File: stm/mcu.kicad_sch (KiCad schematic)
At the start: 33 parts, among them J1 Conn_02x07_Odd_Even, SW2 SW_Push, U1 REF4132B25DBVR, U2 STM32H730ZBTx, Y3 Crystal_GND24, Y4 Crystal

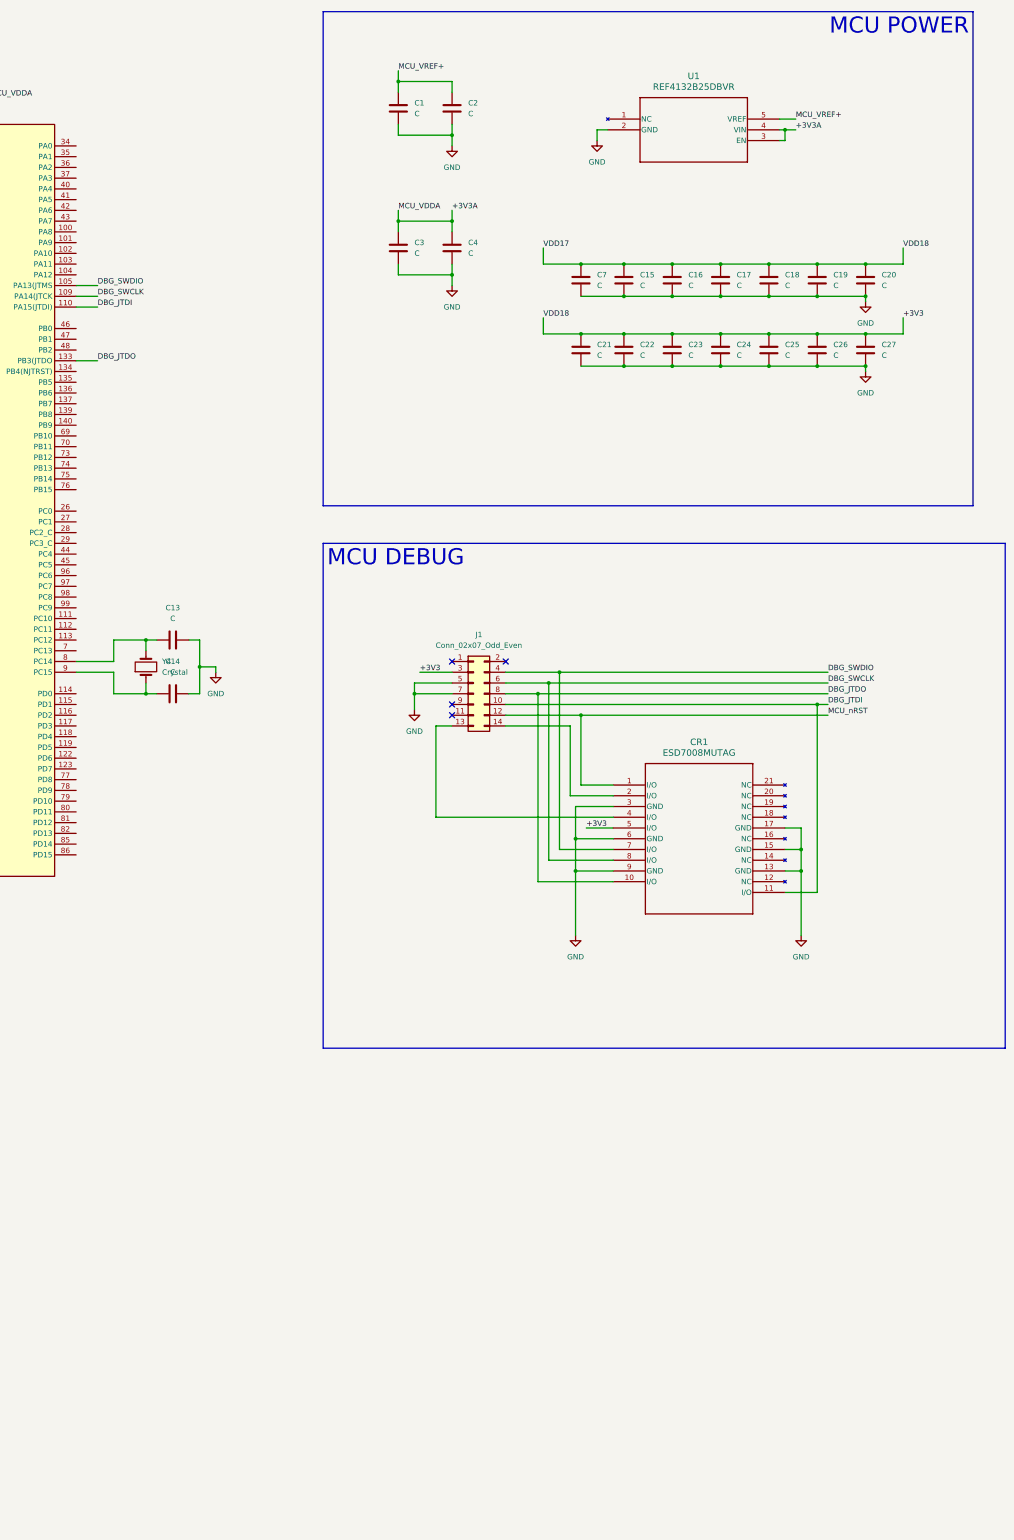
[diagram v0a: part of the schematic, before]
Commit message: STM MCU SD Card
Implemented SD card for external memory.
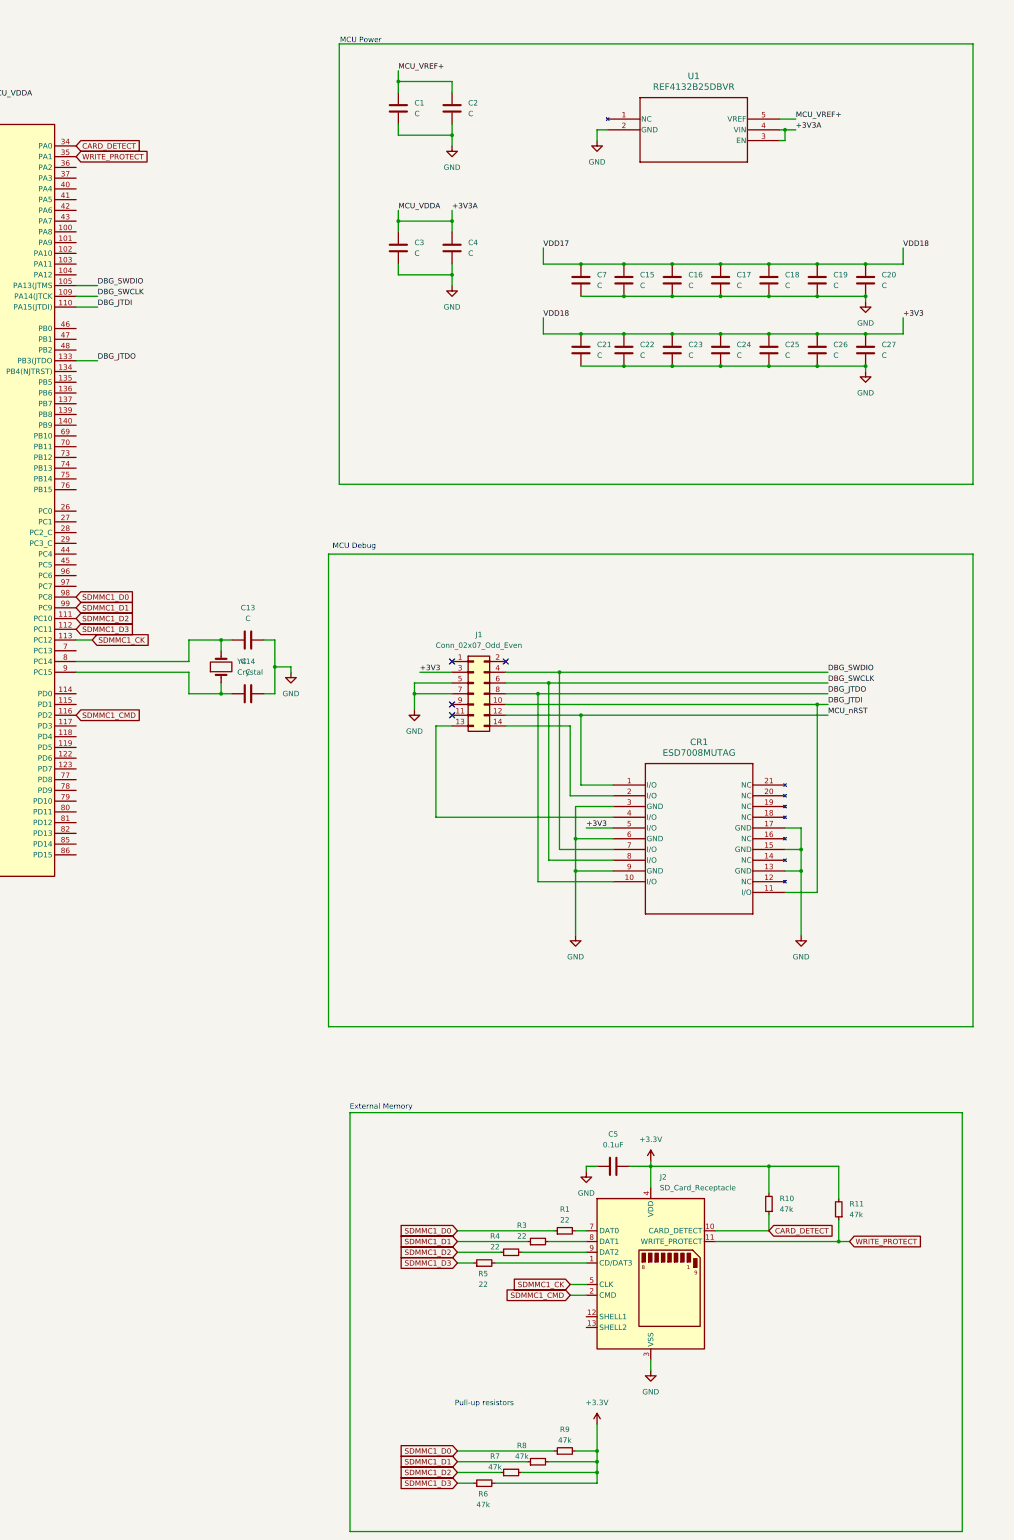
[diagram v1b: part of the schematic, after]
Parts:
- added C5: 0.1uF, symbol Device:C
- added J2: SD_Card_Receptacle, symbol Connector:SD_Card_Receptacle
- added R1, R3, R4, R5: 22, symbol Device:R_Small
- added R10, R11, R6, R7, R8, R9: 47k, symbol Device:R_Small
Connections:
- net GND: now also C5.1, J2.3 (VSS), J2.6 (VSS)
- net SDMMC1_D2: now reaches U2.111 (PC10)
- net SDMMC1_D2: now also R4.1, R7.1
- net SDMMC1_D3: now reaches U2.112 (PC11)
- net SDMMC1_D3: now also R5.1, R6.1
- net SDMMC1_CK: now reaches U2.113 (PC12)
- net SDMMC1_CK: now also J2.5 (CLK)
- net SDMMC1_CMD: now reaches U2.116 (PD2)
- net SDMMC1_CMD: now also J2.2 (CMD)
- net CARD_DETECT: now reaches U2.34 (PA0)
- net CARD_DETECT: now also J2.10 (CARD_DETECT), R10.1
- net WRITE_PROTECT: now reaches U2.35 (PA1)
- net WRITE_PROTECT: now also J2.11 (WRITE_PROTECT), R11.1
- net SDMMC1_D0: now reaches U2.98 (PC8)
- net SDMMC1_D0: now also R1.1, R9.1
- net SDMMC1_D1: now reaches U2.99 (PC9)
- net SDMMC1_D1: now also R3.1, R8.1
- new net: J2.1 (CD/DAT3), R5.2
- new net: J2.7 (DAT0), R1.2
- new net: J2.8 (DAT1), R3.2
- new net: J2.9 (DAT2), R4.2
- new net +3.3V: C5.2, J2.4 (VDD), R10.2, R11.2, R6.2, R7.2, R8.2, R9.2
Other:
- note added: "External Memory"
- note added: "MCU Debug"
- note added: "MCU Power"
- note added: "Pull-up resistors"
- moved on the sheet: C13, C14, Y4

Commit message: ethernet phy
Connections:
- net WRITE_PROTECT: now also U2.56 (PG0); no longer U2.35 (PA1)
- net ETH_MDC: now reaches U2.27 (PC1)
- net ETH_MDIO: now reaches U2.36 (PA2)
- net ETH_CRS_DV: now reaches U2.43 (PA7)
- net ETH_RXD0: now reaches U2.44 (PC4)
- net ETH_RXD1: now reaches U2.45 (PC5)
- net ETH_TX_EN: now reaches U2.70 (PB11)
- net ETH_TXD0: now reaches U2.73 (PB12)
- net ETH_TXD1: now reaches U2.74 (PB13)
- new net ETH_REF_CLK: U2.35 (PA1)

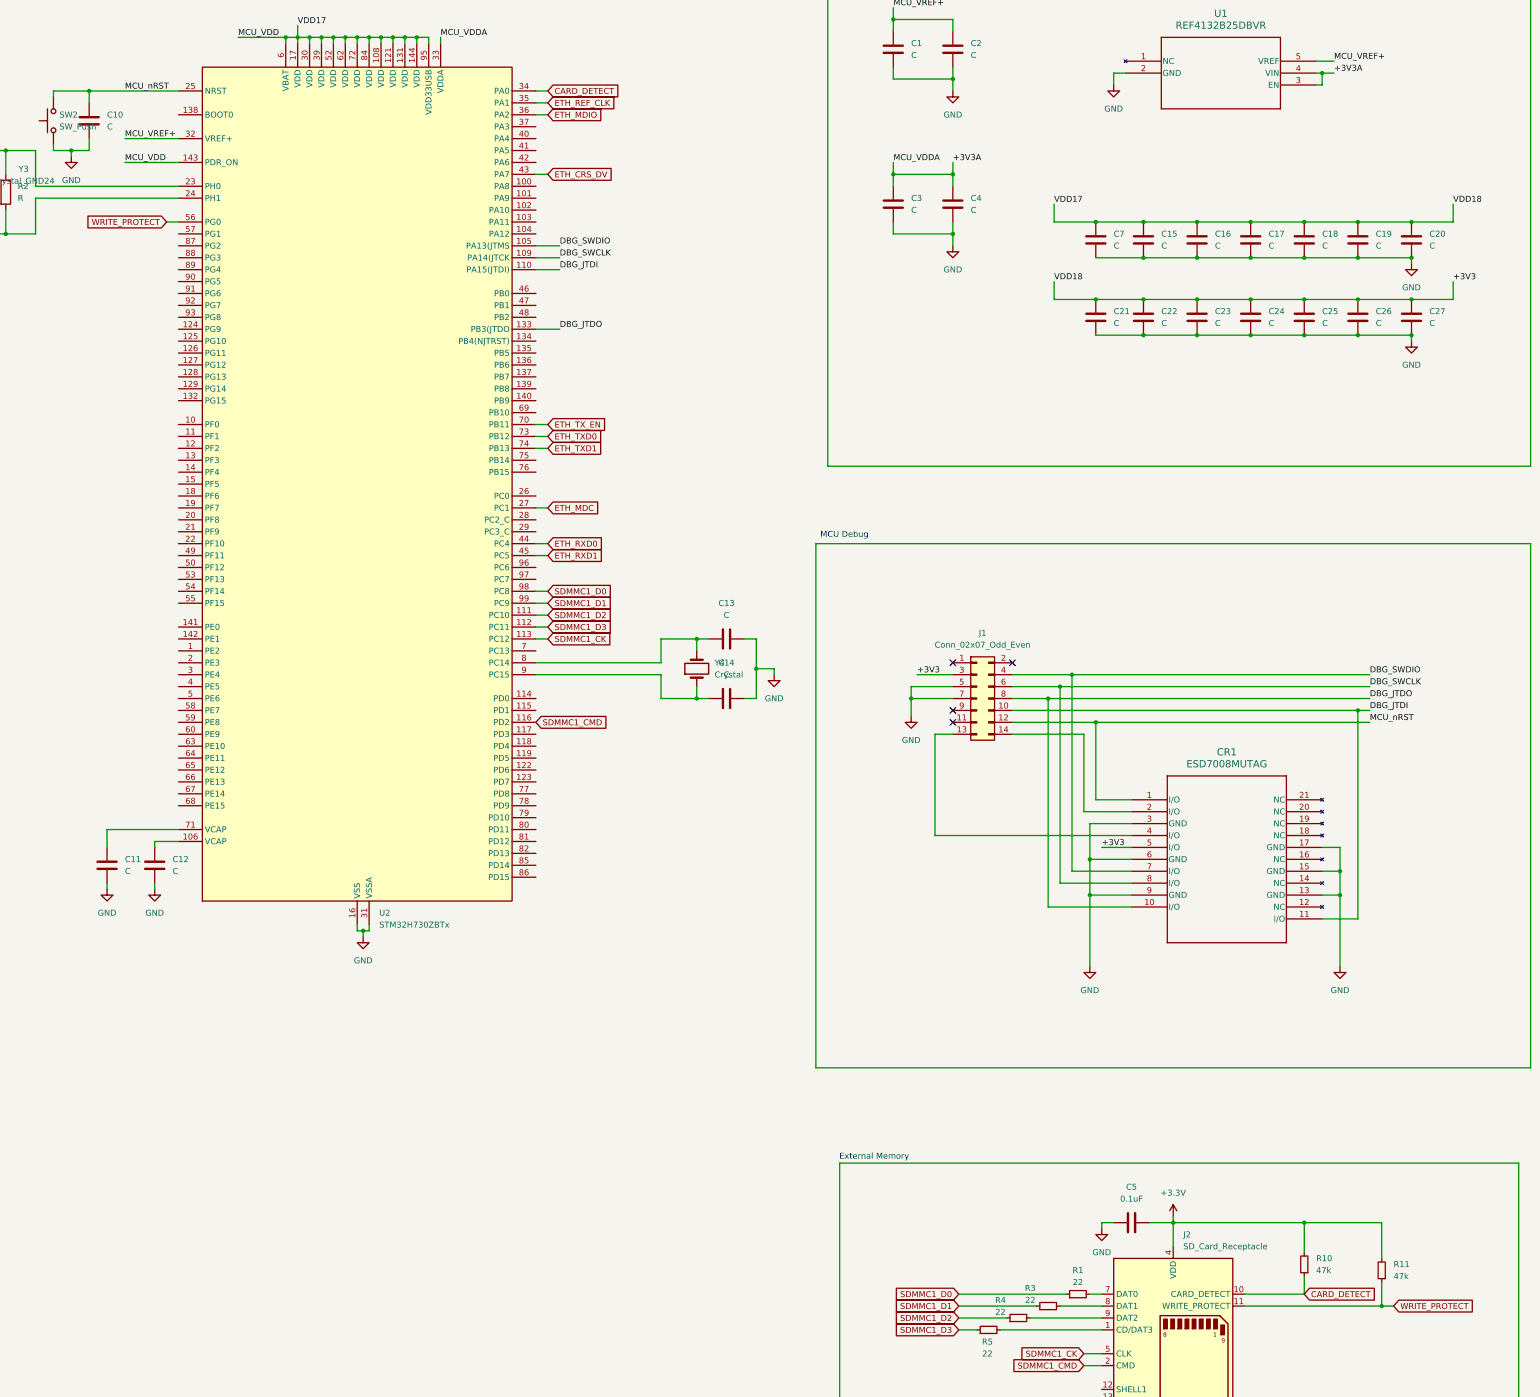
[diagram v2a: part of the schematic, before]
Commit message: usb to uart fix
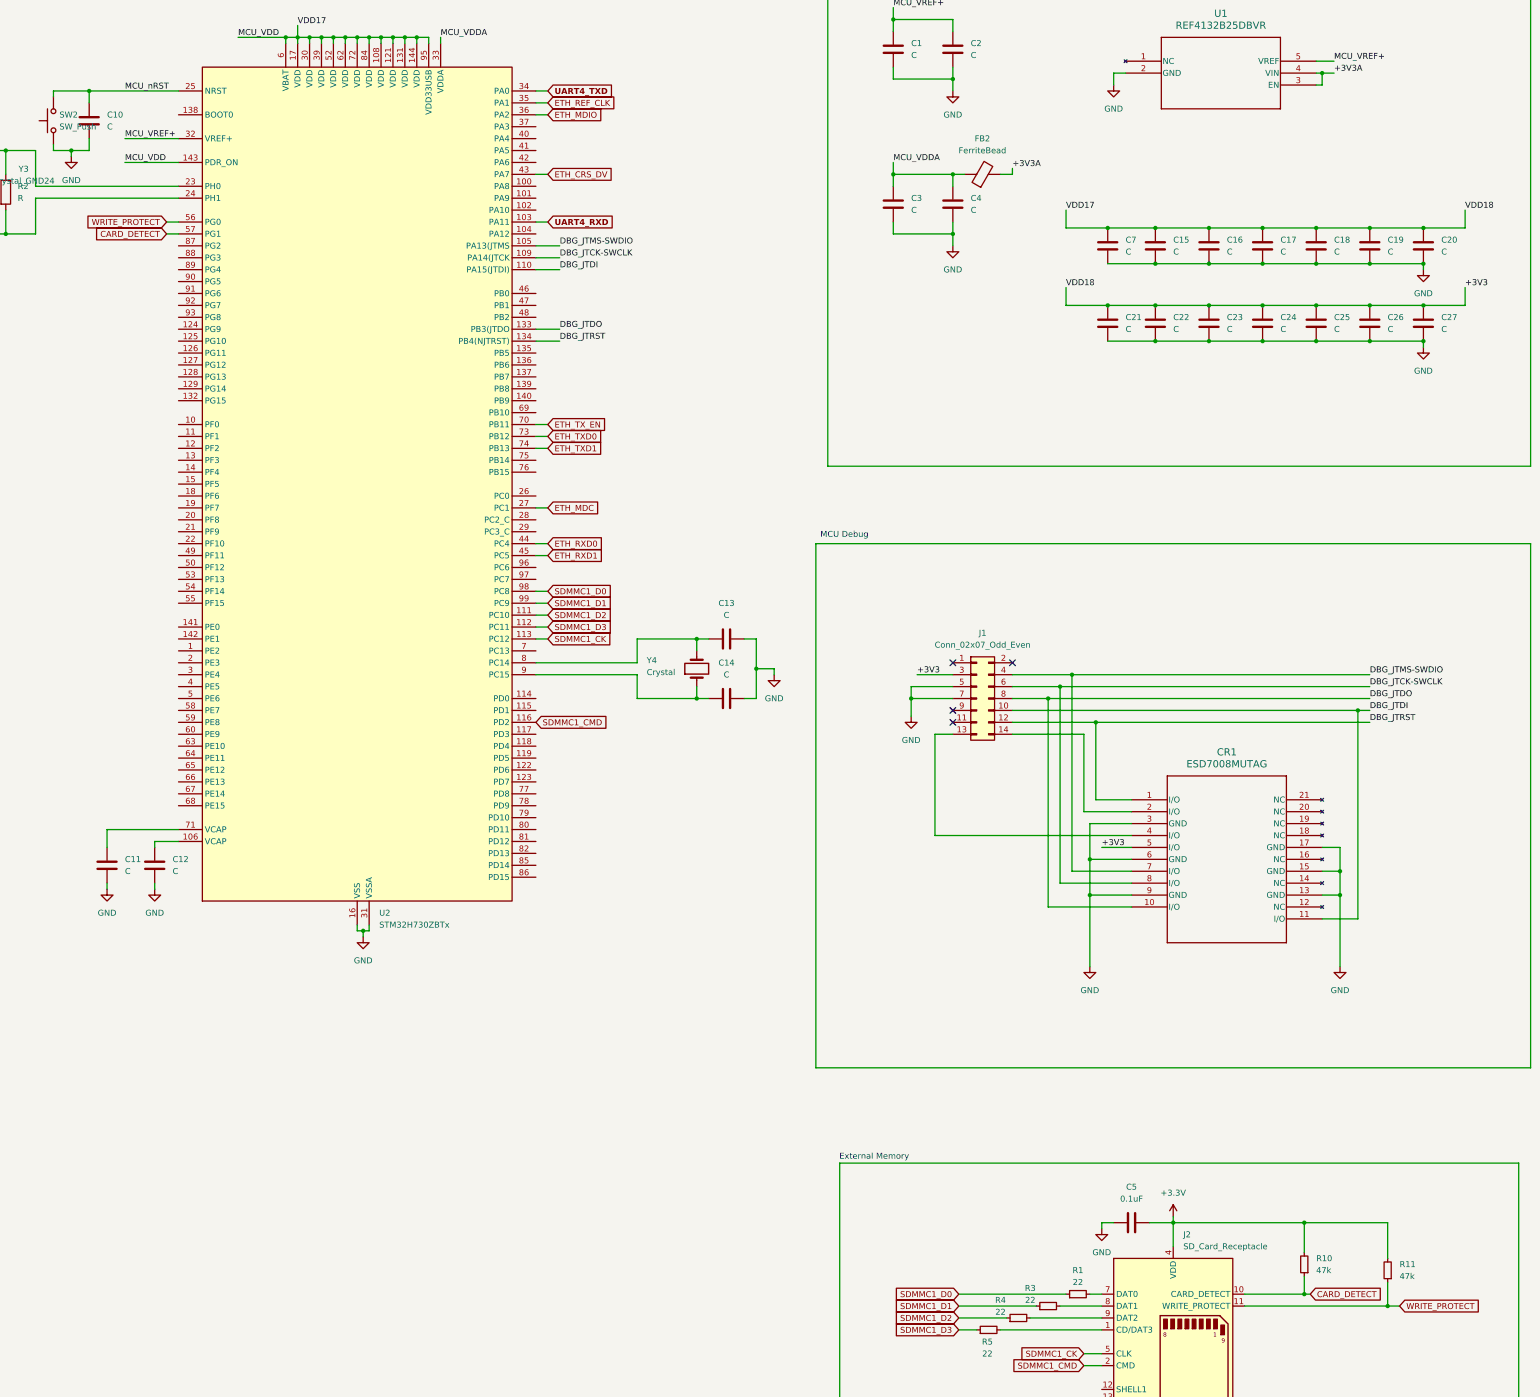
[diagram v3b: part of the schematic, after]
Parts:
- added FB2: FerriteBead, symbol Device:FerriteBead
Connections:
- net +3V3A: now also FB2.2; no longer C3.1, C4.1, U2.33 (VDDA)
- net CARD_DETECT: now also U2.57 (PG1); no longer U2.34 (PA0)
- net MCU_nRST: no longer CR1.1 (I/O), J1.12 (Pin_12)
- net UART4_RXD: now reaches U2.103 (PA11)
- net DBG_JTRST: now reaches U2.134 (PB4(NJTRST))
- net DBG_JTRST: now also CR1.1 (I/O), J1.12 (Pin_12)
- net DBG_SWCLK renamed DBG_JTCK-SWCLK
- net DBG_SWDIO renamed DBG_JTMS-SWDIO
- new net MCU_VDDA: C3.1, C4.1, FB2.1, U2.33 (VDDA)
- new net UART4_TXD: U2.34 (PA0)
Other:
- moved on the sheet: C15, C16, C17, C18, C19, C20, C21, C22, C23, C24, C25, C26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

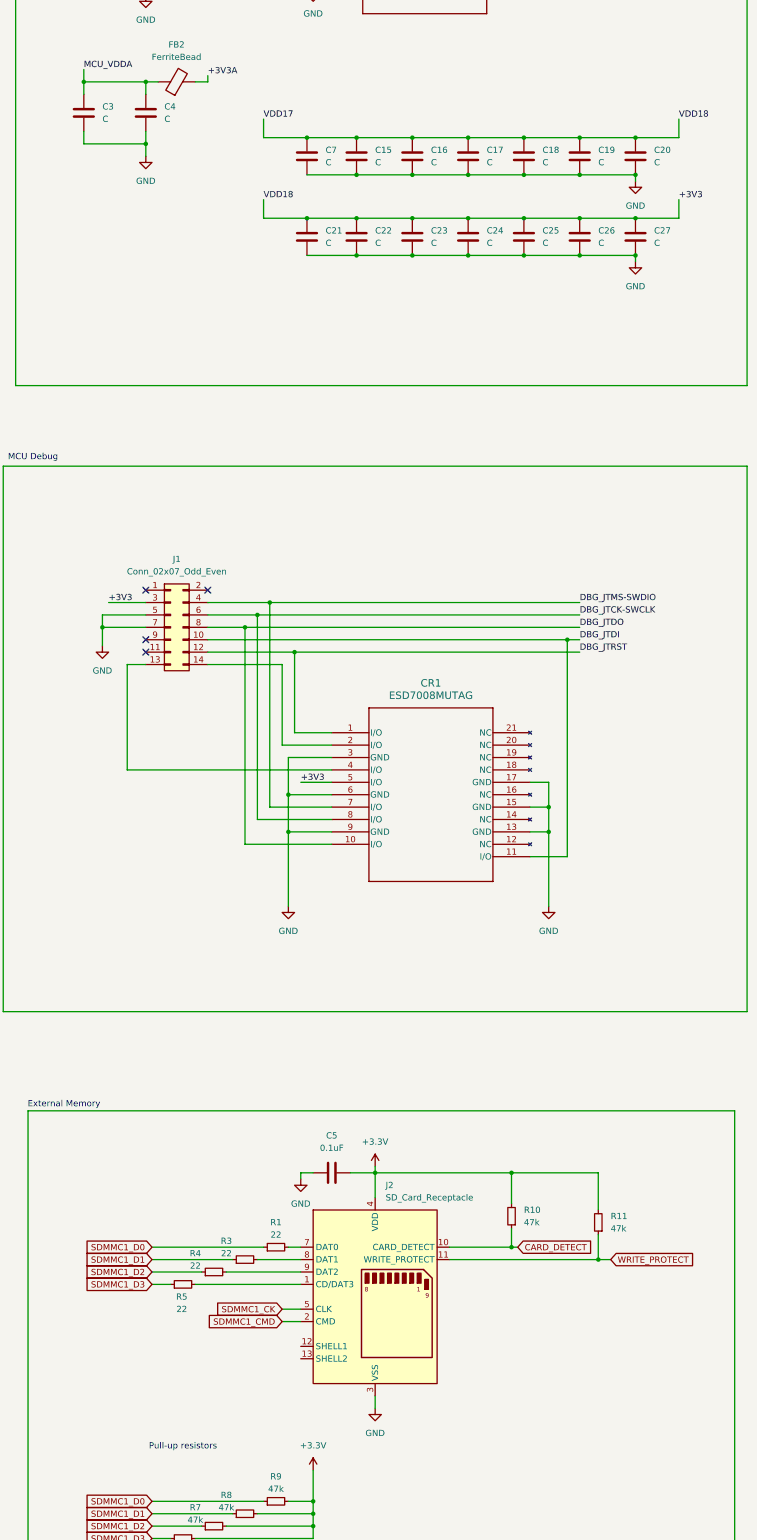
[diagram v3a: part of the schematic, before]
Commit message: changed 3.3V to 3V3
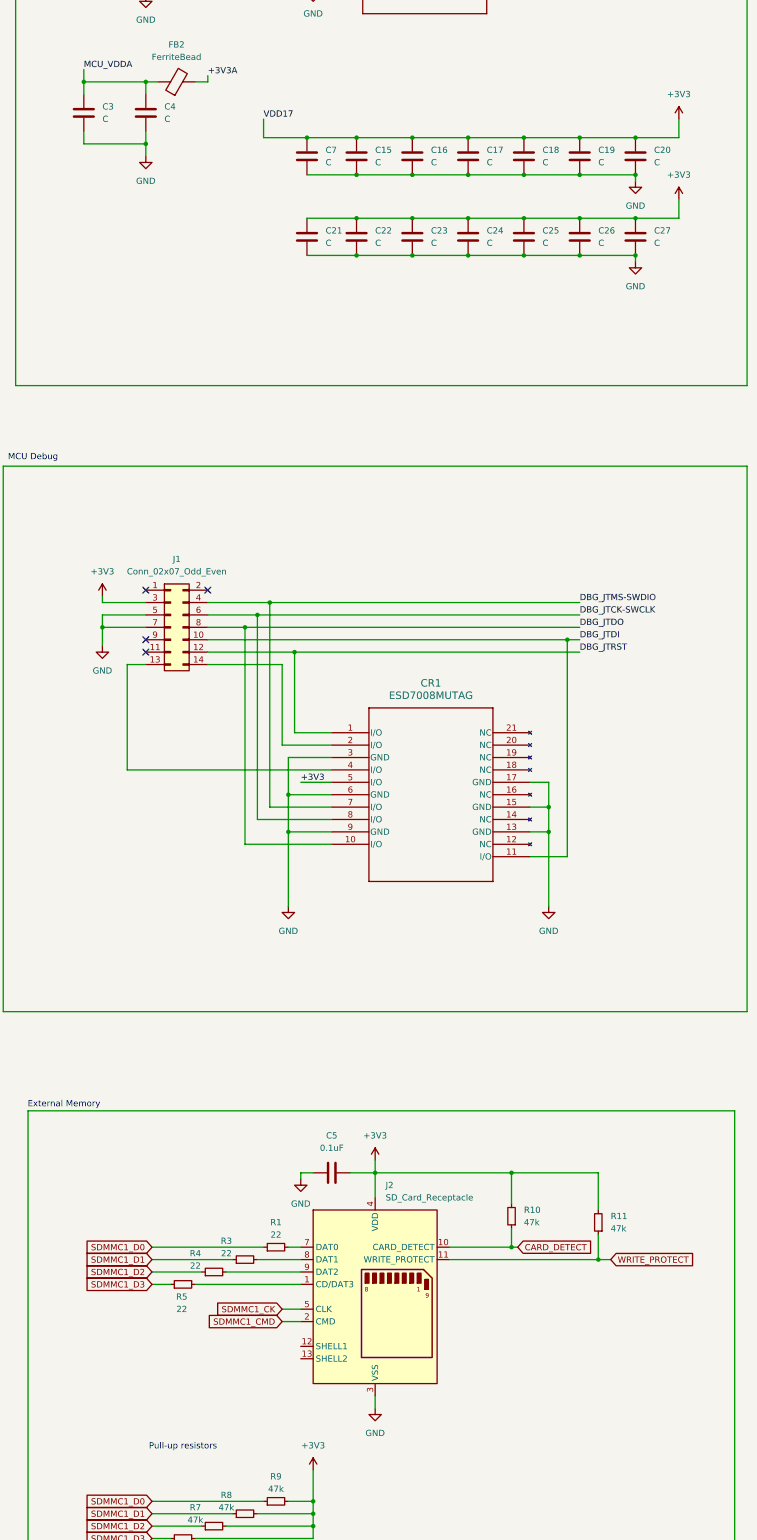
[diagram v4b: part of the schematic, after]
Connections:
- net +3.3V is gone; now on net +3V3: C5.2, J2.4 (VDD), R10.2, R11.2, R6.2, R7.2, R8.2, R9.2
